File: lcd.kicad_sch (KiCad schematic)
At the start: 9 parts, among them J2 FPC-05F-40PH20, Q5 SS8050

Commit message: changes after testing the display
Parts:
- removed R11, R9: 10R, Resistor_SMD:R_0603_1608Metric, symbol Device:R_Small
- J2: LCSC C2856812 -> C262648; Manufacturer XUNPU -> JUSHUO; Manufacturer Part Number FPC-05F-40PH20 -> AFC07-S40ECA-00
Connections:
- net at J2.35 (Pin_35), R10.1: now also J2.34 (Pin_34), J2.36 (Pin_36)
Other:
- note added: "https://www.buydisplay.com/3-2-inch-240x320-ips-tft-lcd-display-optl-capacitive-touchscreen-st7789"
- note removed: "https://nl.aliexpress.com/item/1005008112942872.html"
- note removed: "shield example: https://www.buydisplay.com/3-2-inch-240x320-ips-tft-lcd-module-for-arduino-and-raspberry-pi"
- moved on the sheet: R10
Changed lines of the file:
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@@
 		)
 	)
-	(text "shield example:\nhttps://www.buydisplay.com/3-2-inch-240x320-ips-tft-lcd-module-for-arduino-and-raspberry-pi"
-		(exclude_from_sim no)
-		(at 140.97 22.86 0)
-		(effects
-			(font
-				(size 1.27 1.27)
-			)
-		)
-	)
-	(text "https://nl.aliexpress.com/item/1005008112942872.html"
+	(text "https://www.buydisplay.com/3-2-inch-240x320-ips-tft-lcd-display-optl-capacitive-touchscreen-st7789"
 		(exclude_from_sim no)
 		(at 76.454 48.768 0)
@@
 	)
 	(junction
-		(at 81.28 146.05)
+		(at 77.47 146.05)
 		(diameter 0)
 		(color 0 0 0 0)
@@
 	(wire
 		(pts
+			(xy 74.93 146.05) (xy 77.47 146.05)
+		)
+		(stroke
+			(width 0)
+			(type default)
+		)
+	)
+	(wire
+		(pts
 			(xy 74.93 85.09) (xy 100.33 85.09)
 		)
@@
 	(wire
 		(pts
-			(xy 81.28 143.51) (xy 80.01 143.51)
-		)
-		(stroke
-			(width 0)
-			(type default)
-		)
-	)
-	(wire
-		(pts
 			(xy 87.63 58.42) (xy 87.63 72.39)
 		)
@@
 	(wire
 		(pts
+			(xy 77.47 146.05) (xy 80.01 146.05)
+		)
+		(stroke
+			(width 0)
+			(type default)
+		)
+	)
+	(wire
+		(pts
 			(xy 74.93 156.21) (xy 87.63 156.21)
 		)
@@
 	(wire
 		(pts
+			(xy 74.93 148.59) (xy 77.47 148.59)
+		)
+		(stroke
+			(width 0)
+			(type default)
+		)
+	)
+	(wire
+		(pts
 			(xy 124.46 152.4) (xy 124.46 157.48)
 		)
@@
 	(wire
 		(pts
-			(xy 81.28 146.05) (xy 81.28 148.59)
+			(xy 77.47 146.05) (xy 77.47 148.59)
 		)
 		(stroke
@@
 	(wire
 		(pts
+			(xy 85.09 146.05) (xy 114.3 146.05)
+		)
+		(stroke
+			(width 0)
+			(type default)
+		)
+	)
+	(wire
+		(pts
 			(xy 87.63 168.91) (xy 95.25 168.91)
 		)
@@
 	(wire
 		(pts
-			(xy 81.28 148.59) (xy 80.01 148.59)
+			(xy 74.93 143.51) (xy 77.47 143.51)
 		)
 		(stroke
@@
 	(wire
 		(pts
-			(xy 81.28 146.05) (xy 80.01 146.05)
-		)
-		(stroke
-			(width 0)
-			(type default)
-		)
-	)
-	(wire
-		(pts
 			(xy 74.93 158.75) (xy 87.63 158.75)
 		)
@@
 	(wire
 		(pts
-			(xy 81.28 146.05) (xy 114.3 146.05)
-		)
-		(stroke
-			(width 0)
-			(type default)
-		)
-	)
-	(wire
-		(pts
 			(xy 74.93 153.67) (xy 95.25 153.67)
 		)
@@
 	(wire
 		(pts
-			(xy 81.28 143.51) (xy 81.28 146.05)
+			(xy 77.47 143.51) (xy 77.47 146.05)
 		)
 		(stroke
@@
 	(symbol
 		(lib_id "Device:R_Small")
-		(at 77.47 146.05 90)
+		(at 82.55 146.05 90)
 		(unit 1)
 		(exclude_from_sim no)
@@
 		(dnp no)
 		(property "Reference" "R10"
-			(at 60.96 143.51 90)
+			(at 82.55 142.24 90)
 			(effects
 				(font
@@
 		)
 		(property "Value" "10R"
-			(at 60.96 145.034 90)
+			(at 82.55 144.272 90)
 			(effects
 				(font
@@
 		)
 		(property "Footprint" "Resistor_SMD:R_0603_1608Metric"
-			(at 77.47 146.05 0)
+			(at 82.55 146.05 0)
 			(effects
 				(font
@@
 		)
 		(property "Datasheet" "~"
-			(at 77.47 146.05 0)
+			(at 82.55 146.05 0)
 			(effects
 				(font
@@
 		)
 		(property "Description" "Resistor, small symbol"
-			(at 77.47 146.05 0)
+			(at 82.55 146.05 0)
 			(effects
 				(font
@@
 		)
 		(property "LCSC" ""
-			(at 77.47 146.05 0)
+			(at 82.55 146.05 0)
 			(effects
 				(font
@@
 		)
 		(property "Manufacturer" ""
-			(at 77.47 146.05 0)
+			(at 82.55 146.05 0)
 			(effects
 				(font
@@
 		)
 		(property "Manufacturer Part Number" ""
-			(at 77.47 146.05 0)
+			(at 82.55 146.05 0)
 			(effects
 				(font
@@
 	)
 	(symbol
-		(lib_id "Device:R_Small")
-		(at 77.47 143.51 90)
-		(unit 1)
-		(exclude_from_sim no)
-		(in_bom yes)
-		(on_board yes)
-		(dnp no)
-		(property "Reference" "R9"
-			(at 66.04 141.224 90)
-			(effects
-				(font
-					(size 1.27 1.27)
-				)
-			)
-		)
-		(property "Value" "10R"
-			(at 66.04 142.748 90)
-			(effects
-				(font
-					(size 1.27 1.27)
-				)
-			)
-		)
-		(property "Footprint" "Resistor_SMD:R_0603_1608Metric"
-			(at 77.47 143.51 0)
-			(effects
-				(font
-					(size 1.27 1.27)
-				)
-				(hide yes)
-			)
-		)
-		(property "Datasheet" "~"
-			(at 77.47 143.51 0)
-			(effects
-				(font
-					(size 1.27 1.27)
-				)
-				(hide yes)
-			)
-		)
-		(property "Description" "Resistor, small symbol"
-			(at 77.47 143.51 0)
-			(effects
-				(font
-					(size 1.27 1.27)
-				)
-				(hide yes)
-			)
-		)
-		(property "LCSC" ""
-			(at 77.47 143.51 0)
-			(effects
-				(font
-					(size 1.27 1.27)
-				)
-				(hide yes)
-			)
-		)
-		(property "Manufacturer" ""
-			(at 77.47 143.51 0)
-			(effects
-				(font
-					(size 1.27 1.27)
-				)
-				(hide yes)
-			)
-		)
-		(property "Manufacturer Part Number" ""
-			(at 77.47 143.51 0)
-			(effects
-				(font
-					(size 1.27 1.27)
-				)
-				(hide yes)
-			)
-		)
-		(pin "1"
-		)
-		(pin "2"
-		)
-		(instances
-			(project ""
-				(path "/f4643692-c319-40a7-82a2-3e775c0a417f/d0993c89-522c-4206-a2f2-b5b66c7e7b73"
-					(reference "R9")
-					(unit 1)
-				)
-			)
-		)
-	)
-	(symbol
-		(lib_id "Device:R_Small")
-		(at 77.47 148.59 90)
-		(unit 1)
-		(exclude_from_sim no)
-		(in_bom yes)
-		(on_board yes)
-		(dnp no)
-		(property "Reference" "R11"
-			(at 66.04 146.304 90)
-			(effects
-				(font
-					(size 1.27 1.27)
-				)
-			)
-		)
-		(property "Value" "10R"
-			(at 66.04 147.828 90)
-			(effects
-				(font
-					(size 1.27 1.27)
-				)
-			)
-		)
-		(property "Footprint" "Resistor_SMD:R_0603_1608Metric"
-			(at 77.47 148.59 0)
-			(effects
-				(font
-					(size 1.27 1.27)
-				)
-				(hide yes)
-			)
-		)
-		(property "Datasheet" "~"
-			(at 77.47 148.59 0)
-			(effects
-				(font
-					(size 1.27 1.27)
-				)
-				(hide yes)
-			)
-		)
-		(property "Description" "Resistor, small symbol"
-			(at 77.47 148.59 0)
-			(effects
-				(font
-					(size 1.27 1.27)
-				)
-				(hide yes)
-			)
-		)
-		(property "LCSC" ""
-			(at 77.47 148.59 0)
-			(effects
-				(font
-					(size 1.27 1.27)
-				)
-				(hide yes)
-			)
-		)
-		(property "Manufacturer" ""
-			(at 77.47 148.59 0)
-			(effects
-				(font
-					(size 1.27 1.27)
-				)
-				(hide yes)
-			)
-		)
-		(property "Manufacturer Part Number" ""
-			(at 77.47 148.59 0)
-			(effects
-				(font
-					(size 1.27 1.27)
-				)
-				(hide yes)
-			)
-		)
-		(pin "1"
-		)
-		(pin "2"
-		)
-		(instances
-			(project "gameboy"
-				(path "/f4643692-c319-40a7-82a2-3e775c0a417f/d0993c89-522c-4206-a2f2-b5b66c7e7b73"
-					(reference "R11")
-					(unit 1)
-				)
-			)
-		)
-	)
-	(symbol
 		(lib_id "Connector_Generic_MountingPin:Conn_01x40_MountingPin")
 		(at 69.85 107.95 0)
@@
 			)
 		)
-		(property "LCSC" "C2856812"
+		(property "LCSC" "C262648"
 			(at 69.85 107.95 0)
 			(effects
@@
 			)
 		)
-		(property "Manufacturer" "XUNPU"
+		(property "Manufacturer" "JUSHUO"
 			(at 69.85 107.95 0)
 			(effects
@@
 			)
 		)
-		(property "Manufacturer Part Number" "FPC-05F-40PH20"
+		(property "Manufacturer Part Number" "AFC07-S40ECA-00"
 			(at 69.85 107.95 0)
 			(effects

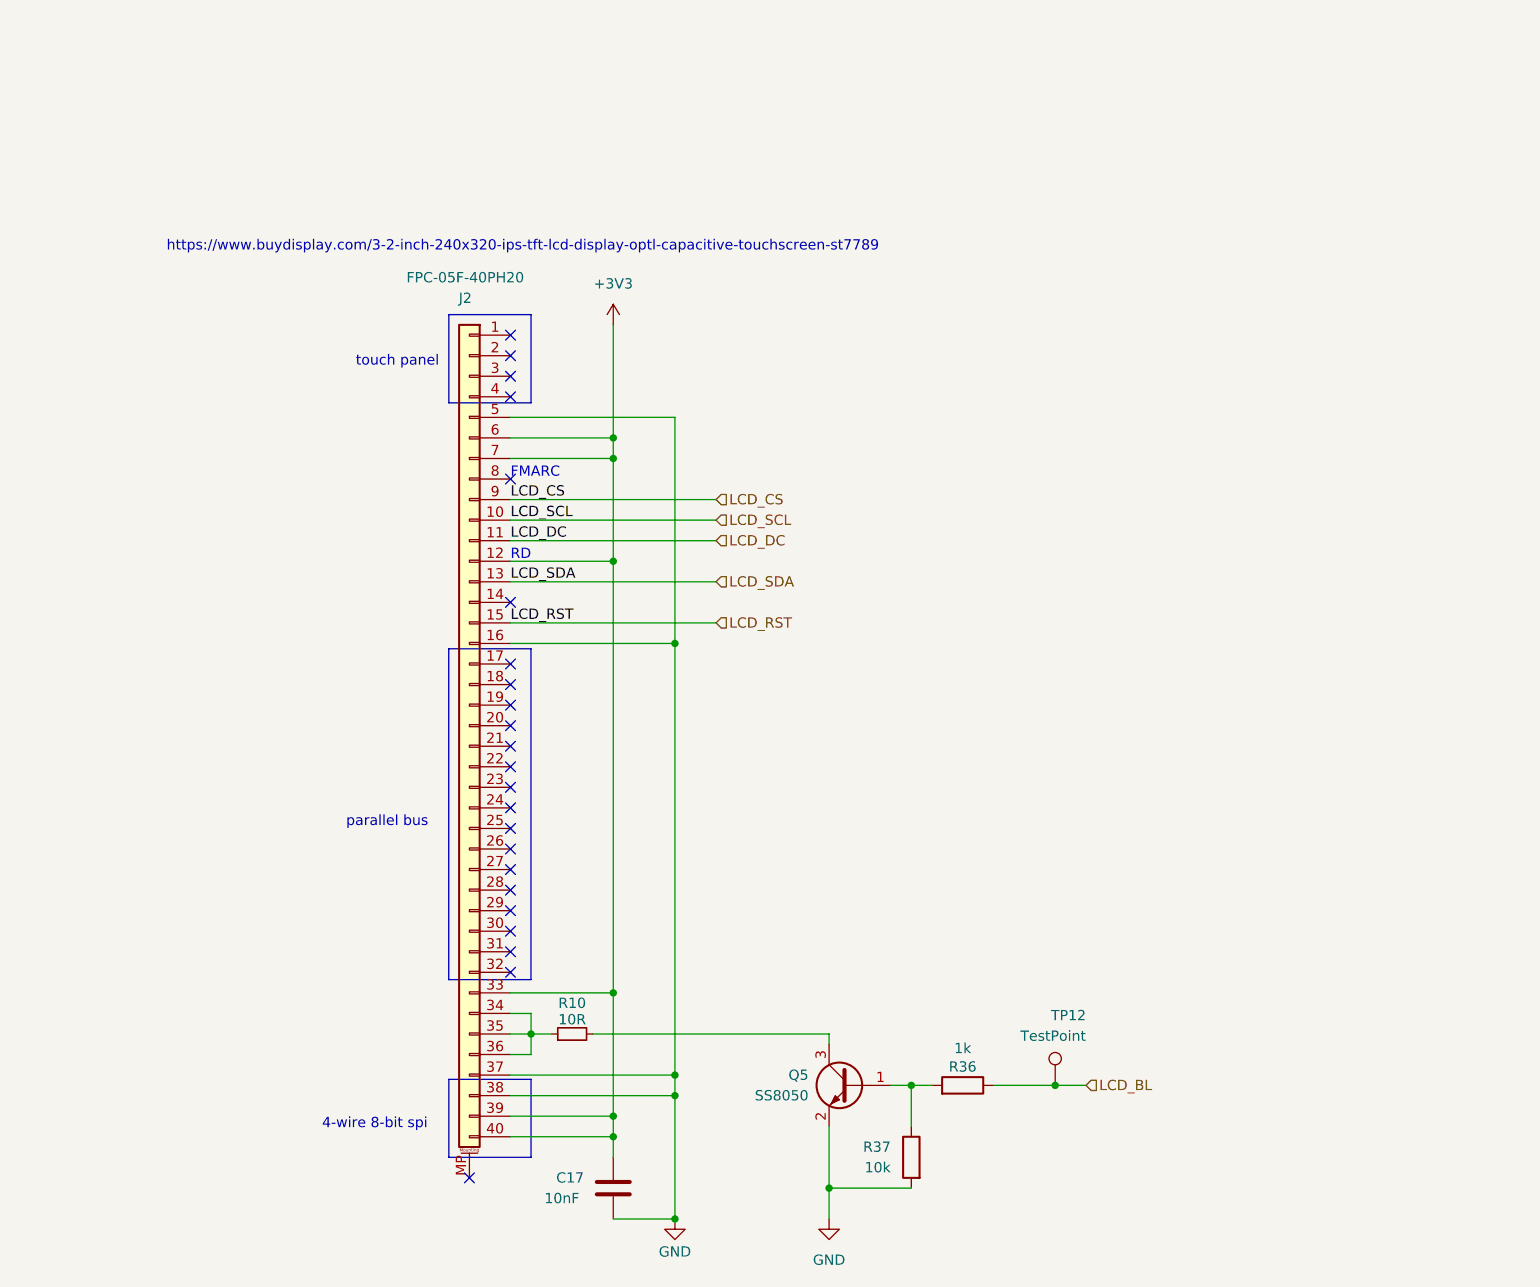
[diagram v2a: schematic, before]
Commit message: fix lcd connector orientation
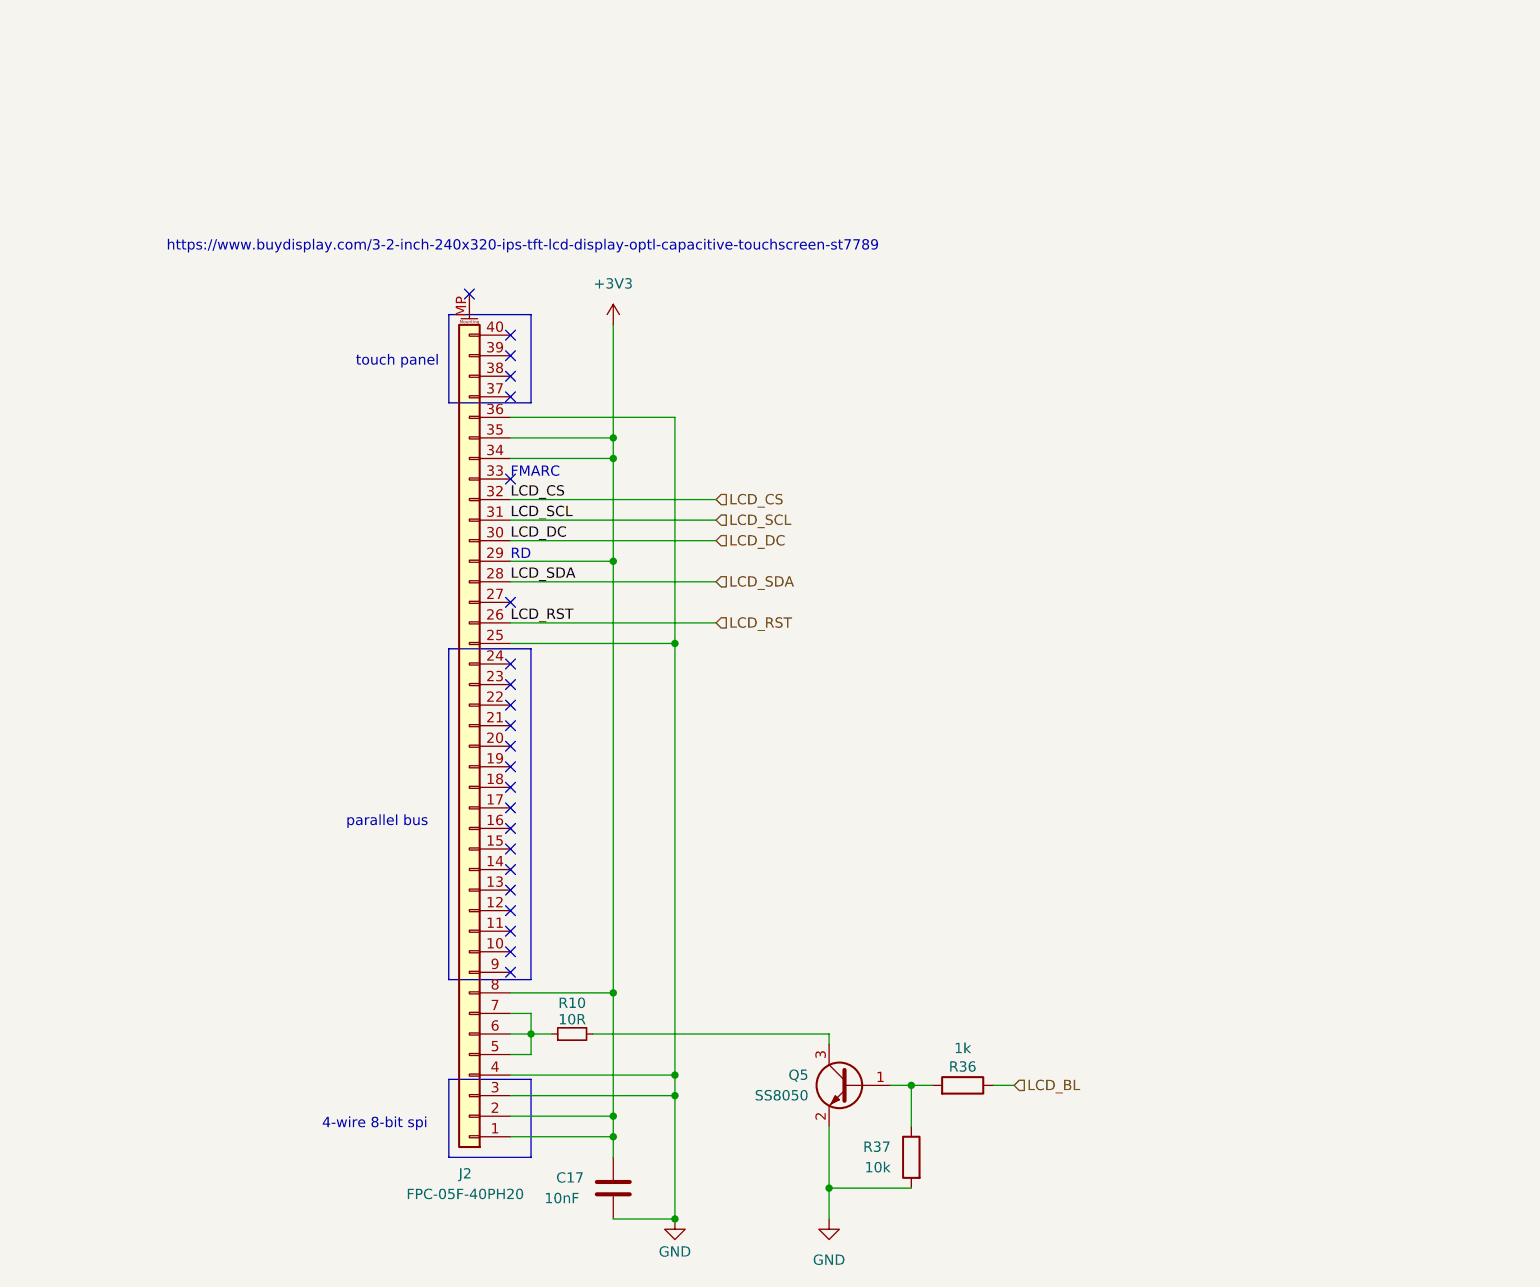
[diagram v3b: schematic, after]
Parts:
- removed TP12: TestPoint, TestPoint:TestPoint_Pad_D1.0mm, symbol Connector:TestPoint
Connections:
- net +3V3: now also J2.1 (Pin_1), J2.2 (Pin_2), J2.29 (Pin_29), J2.34 (Pin_34), J2.35 (Pin_35), J2.8 (Pin_8); no longer J2.12 (Pin_12), J2.33 (Pin_33), J2.39 (Pin_39), J2.40 (Pin_40), J2.6 (Pin_6), J2.7 (Pin_7)
- net GND: now also J2.25 (Pin_25), J2.3 (Pin_3), J2.36 (Pin_36), J2.4 (Pin_4); no longer J2.16 (Pin_16), J2.37 (Pin_37), J2.38 (Pin_38), J2.5 (Pin_5)
- net LCD_CS: now also J2.32 (Pin_32); no longer J2.9 (Pin_9)
- net LCD_DC: now also J2.30 (Pin_30); no longer J2.11 (Pin_11)
- net LCD_RST: now also J2.26 (Pin_26); no longer J2.15 (Pin_15)
- net LCD_SCL: now also J2.31 (Pin_31); no longer J2.10 (Pin_10)
- net LCD_SDA: now also J2.28 (Pin_28); no longer J2.13 (Pin_13)
- new net: J2.5 (Pin_5), J2.6 (Pin_6), J2.7 (Pin_7), R10.1
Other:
- moved on the sheet: J2
